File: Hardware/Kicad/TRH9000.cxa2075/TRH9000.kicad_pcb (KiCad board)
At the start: 4 copper layers, 100 x 77.5 mm, 66 parts, among them J1 S-Video, J2 RGB, Q1 BC817, U1 74HC138, U2 74HC32, U3 V9990, U4 KM428C256, U5 KM428C256, U6 CXA2075M, X1 14.31818MHz, Y1 21.47727Mhz

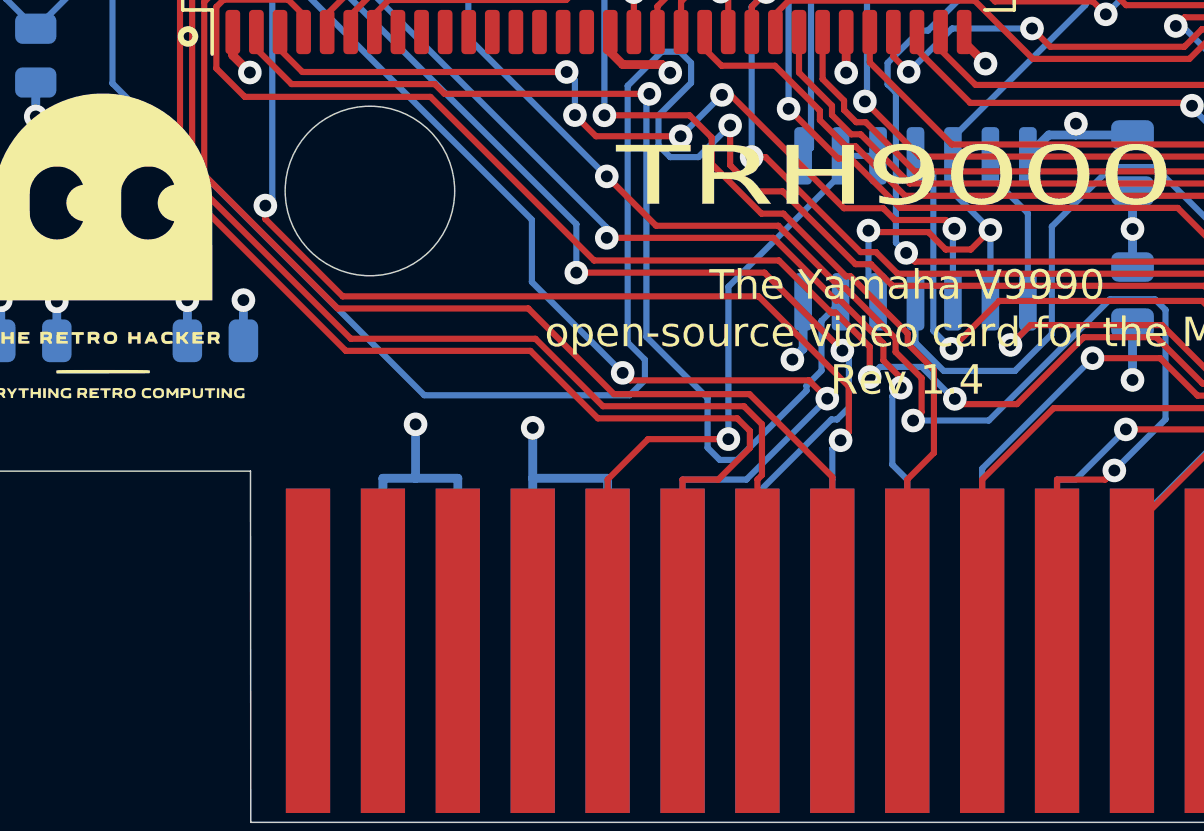
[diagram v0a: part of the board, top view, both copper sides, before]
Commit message: SW1-SW2 jumper. v1.41
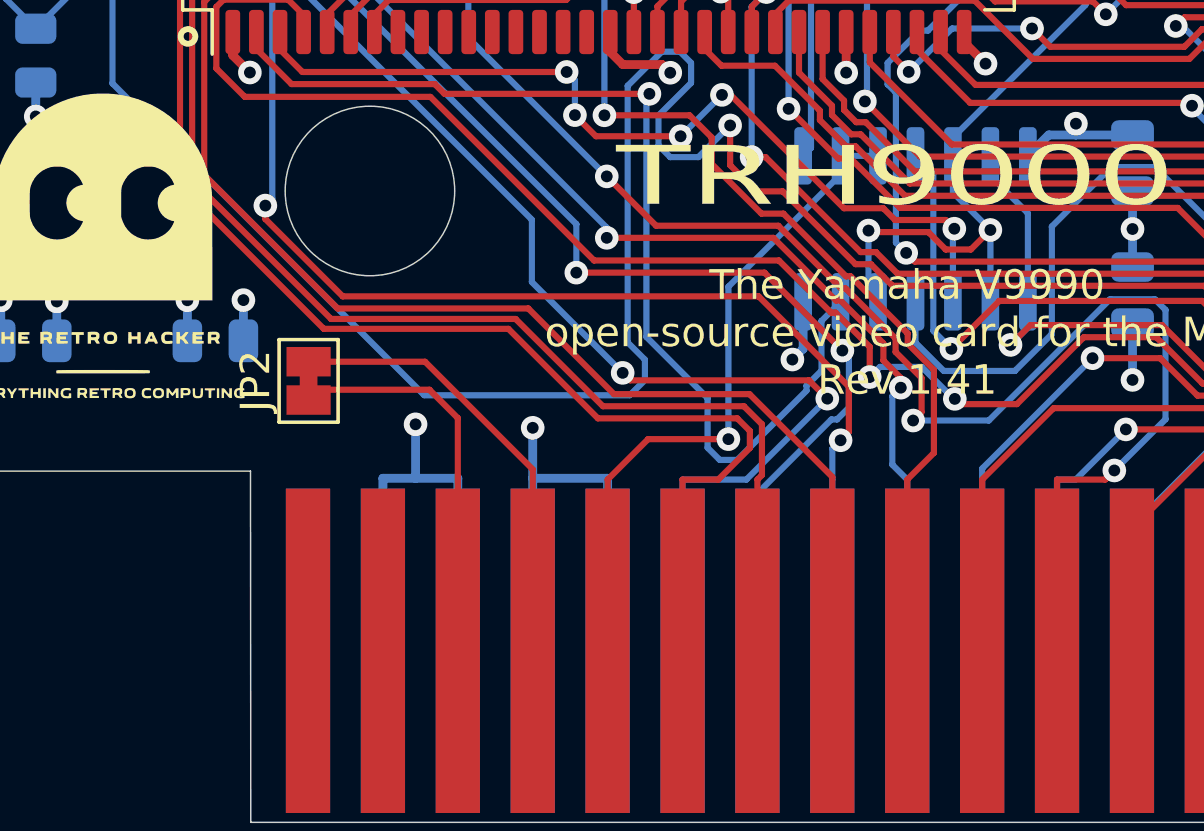
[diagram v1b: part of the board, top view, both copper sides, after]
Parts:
- added JP2: Jumper_2_Bridged, Jumper:SolderJumper-2_P1.3mm_Bridged_Pad1.0x1.5mm, F.Cu at (126.6, 118.5)
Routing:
- net /SW1: track 0.00 -> 15.3 mm
- net /SW2: track 0.00 -> 13.5 mm
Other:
- board text added: "The Yamaha V9990 open-source video card for the MSX Rev 1.41"
- board text removed: "The Yamaha V9990 open-source video card for the MSX Rev 1.4"
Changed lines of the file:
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@@
   (paper "A4")
   (title_block
-    (date "2023-11-05")
-    (rev "1.4")
+    (date "2023-12-31")
+    (rev "1.41")
     (company "The Retro Hacker")
     (comment 2 "Shared under CERN-OHL-S license")
@@
     )
   )
+  (footprint "Jumper:SolderJumper-2_P1.3mm_Bridged_Pad1.0x1.5mm" (layer "F.Cu")
+    (at 126.6 118.5 90)
+    (descr "SMD Solder Jumper, 1x1.5mm Pads, 0.3mm gap, bridged with 1 copper strip")
+    (tags "net tie solder jumper bridged")
+    (property "Sheetfile" "TRH9000.kicad_sch")
+    (property "Sheetname" "")
+    (property "ki_description" "Jumper, 2-pole, closed/bridged")
+    (property "ki_keywords" "Jumper SPST")
+    (attr exclude_from_pos_files)
+    (net_tie_pad_groups "1, 2")
+    (fp_text reference "JP2" (at 0 -1.8 90) (layer "F.SilkS")
+        (effects (font (size 1 1) (thickness 0.15)))
+    )
+    (fp_text value "Jumper_2_Bridged" (at 0 1.9 90) (layer "F.Fab") hide
+        (effects (font (size 1 1) (thickness 0.15)))
+    )
+    (fp_poly
+      (pts
+        (xy -0.25 -0.3)
+        (xy 0.25 -0.3)
+        (xy 0.25 0.3)
+        (xy -0.25 0.3)
+      )
+      (stroke (width 0) (type solid)) (fill solid) (layer "F.Cu"))
+    (fp_line (start -1.4 -1) (end 1.4 -1)
+      (stroke (width 0.12) (type solid)) (layer "F.SilkS"))
+    (fp_line (start -1.4 1) (end -1.4 -1)
+      (stroke (width 0.12) (type solid)) (layer "F.SilkS"))
+    (fp_line (start 1.4 -1) (end 1.4 1)
+      (stroke (width 0.12) (type solid)) (layer "F.SilkS"))
+    (fp_line (start 1.4 1) (end -1.4 1)
+      (stroke (width 0.12) (type solid)) (layer "F.SilkS"))
+    (fp_line (start -1.65 -1.25) (end -1.65 1.25)
+      (stroke (width 0.05) (type solid)) (layer "F.CrtYd"))
+    (fp_line (start -1.65 -1.25) (end 1.65 -1.25)
+      (stroke (width 0.05) (type solid)) (layer "F.CrtYd"))
+    (fp_line (start 1.65 1.25) (end -1.65 1.25)
+      (stroke (width 0.05) (type solid)) (layer "F.CrtYd"))
+    (fp_line (start 1.65 1.25) (end 1.65 -1.25)
+      (stroke (width 0.05) (type solid)) (layer "F.CrtYd"))
+    (pad "1" smd rect (at -0.65 0 90) (size 1 1.5) (layers "F.Cu" "F.Mask")
+      (net 27 "/SW2") (pinfunction "A") (pintype "passive"))
+    (pad "2" smd rect (at 0.65 0 90) (size 1 1.5) (layers "F.Cu" "F.Mask")
+      (net 28 "/SW1") (pinfunction "B") (pintype "passive"))
+  )
   (footprint "Capacitor_SMD:C_0805_2012Metric" (layer "F.Cu")
     (at 195.54 86.21 -90)
@@
     (effects (font (size 1 1) (thickness 0.15)))
   )
-  (gr_text "The Yamaha V9990 \nopen-source video card for the MSX\nRev 1.4" (at 146.9 116.86) (layer "F.SilkS")
+  (gr_text "The Yamaha V9990 \nopen-source video card for the MSX\nRev 1.41" (at 146.9 116.86) (layer "F.SilkS")
     (effects (font (size 1 1) (thickness 0.15)))
   )
@@
   (segment (start 139.28 127.653) (end 139.28 121.8477) (width 0.21) (layer "B.Cu") (net 26))
   (segment (start 120.2258 99.2641) (end 120.4017 99.2641) (width 0.21) (layer "B.Cu") (net 26))
-  (segment (start 134.1222 117.4818) (end 136.4104 119.77) (width 0.21) (layer "F.Cu") (net 29))
-  (segment (start 139.28 127.653) (end 139.28 121.8477) (width 0.21) (layer "F.Cu") (net 29))
-  (segment (start 122.2406 105.3092) (end 122.2406 111.859) (width 0.21) (layer "F.Cu") (net 29))
-  (segment (start 122.2013 98.62) (end 122.6506 99.0693) (width 0.21) (layer "F.Cu") (net 29))
-  (segment (start 136.4104 119.77) (end 141.1359 119.77) (width 0.21) (layer "F.Cu") (net 29))
+  (segment (start 130.7 118.8) (end 131.66 119.76) (width 0.21) (layer "F.Cu") (net 27))
+  (segment (start 126.6 119.15) (end 126.95 118.8) (width 0.21) (layer "F.Cu") (net 27))
+  (segment (start 126.95 118.8) (end 130.7 118.8) (width 0.21) (layer "F.Cu") (net 27))
+  (segment (start 131.66 119.76) (end 131.66 127.653) (width 0.21) (layer "F.Cu") (net 27))
+  (segment (start 130.55 117.85) (end 134.2 121.5) (width 0.21) (layer "F.Cu") (net 28))
+  (segment (start 134.2 121.5) (end 134.2 127.653) (width 0.21) (layer "F.Cu") (net 28))
+  (segment (start 126.6 117.85) (end 130.55 117.85) (width 0.21) (layer "F.Cu") (net 28))
+  (segment (start 139.28 121.8477) (end 139.28 127.653) (width 0.21) (layer "F.Cu") (net 29))
+  (segment (start 140.4917 121.8477) (end 139.28 121.8477) (width 0.21) (layer "F.Cu") (net 29))
+  (segment (start 121.58 98.62) (end 122.2013 98.62) (width 0.21) (layer "F.Cu") (net 29))
   (segment (start 122.6506 104.8992) (end 122.2406 105.3092) (width 0.21) (layer "F.Cu") (net 29))
+  (segment (start 136.4104 119.77) (end 141.1359 119.77) (width 0.21) (layer "F.Cu") (net 29))
+  (segment (start 122.2406 111.859) (end 127.1166 116.735) (width 0.21) (layer "F.Cu") (net 29))
   (segment (start 141.5636 120.1977) (end 141.5636 120.7758) (width 0.21) (layer "F.Cu") (net 29))
-  (segment (start 121.58 98.62) (end 122.2013 98.62) (width 0.21) (layer "F.Cu") (net 29))
-  (segment (start 122.2406 111.859) (end 127.8634 117.4818) (width 0.21) (layer "F.Cu") (net 29))
-  (segment (start 140.4917 121.8477) (end 139.28 121.8477) (width 0.21) (layer "F.Cu") (net 29))
-  (segment (start 127.8634 117.4818) (end 134.1222 117.4818) (width 0.21) (layer "F.Cu") (net 29))
+  (segment (start 133.3754 116.735) (end 136.4104 119.77) (width 0.21) (layer "F.Cu") (net 29))
   (segment (start 122.6506 99.0693) (end 122.6506 104.8992) (width 0.21) (layer "F.Cu") (net 29))
-  (segment (start 141.1359 119.77) (end 141.5636 120.1977) (width 0.21) (layer "F.Cu") (net 29))
   (segment (start 141.5636 120.7758) (end 140.4917 121.8477) (width 0.21) (layer "F.Cu") (net 29))
+  (segment (start 122.2406 105.3092) (end 122.2406 111.859) (width 0.21) (layer "F.Cu") (net 29))
+  (segment (start 127.1166 116.735) (end 133.3754 116.735) (width 0.21) (layer "F.Cu") (net 29))
+  (segment (start 122.2013 98.62) (end 122.6506 99.0693) (width 0.21) (layer "F.Cu") (net 29))
+  (segment (start 141.1359 119.77) (end 141.5636 120.1977) (width 0.21) (layer "F.Cu") (net 29))
+  (segment (start 141.3627 119.3597) (end 141.974 119.971) (width 0.21) (layer "F.Cu") (net 30))
+  (segment (start 133.6207 116.4) (end 136.5804 119.3597) (width 0.21) (layer "F.Cu") (net 30))
   (segment (start 121.58 97.02) (end 122.1445 97.02) (width 0.21) (layer "F.Cu") (net 30))
   (segment (start 122.1445 97.02) (end 123.0609 97.9364) (width 0.21) (layer "F.Cu") (net 30))
-  (segment (start 141.974 121.6937) (end 141.82 121.8477) (width 0.21) (layer "F.Cu") (net 30))
-  (segment (start 122.6509 111.689) (end 128.0333 117.0714) (width 0.21) (layer "F.Cu") (net 30))
-  (segment (start 141.3627 119.3597) (end 141.974 119.971) (width 0.21) (layer "F.Cu") (net 30))
-  (segment (start 141.82 127.653) (end 141.82 121.8477) (width 0.21) (layer "F.Cu") (net 30))
+  (segment (start 141.82 121.8477) (end 141.82 127.653) (width 0.21) (layer "F.Cu") (net 30))
+  (segment (start 127.3619 116.4) (end 133.6207 116.4) (width 0.21) (layer "F.Cu") (net 30))
   (segment (start 123.0609 105.0692) (end 122.6509 105.4792) (width 0.21) (layer "F.Cu") (net 30))
-  (segment (start 134.2921 117.0714) (end 136.5804 119.3597) (width 0.21) (layer "F.Cu") (net 30))
-  (segment (start 123.0609 97.9364) (end 123.0609 105.0692) (width 0.21) (layer "F.Cu") (net 30))
+  (segment (start 122.6509 111.689) (end 127.3619 116.4) (width 0.21) (layer "F.Cu") (net 30))
+  (segment (start 136.5804 119.3597) (end 141.3627 119.3597) (width 0.21) (layer "F.Cu") (net 30))
   (segment (start 141.974 119.971) (end 141.974 121.6937) (width 0.21) (layer "F.Cu") (net 30))
   (segment (start 122.6509 105.4792) (end 122.6509 111.689) (width 0.21) (layer "F.Cu") (net 30))
-  (segment (start 136.5804 119.3597) (end 141.3627 119.3597) (width 0.21) (layer "F.Cu") (net 30))
-  (segment (start 128.0333 117.0714) (end 134.2921 117.0714) (width 0.21) (layer "F.Cu") (net 30))
+  (segment (start 123.0609 97.9364) (end 123.0609 105.0692) (width 0.21) (layer "F.Cu") (net 30))
+  (segment (start 141.974 121.6937) (end 141.82 121.8477) (width 0.21) (layer "F.Cu") (net 30))
   (segment (start 123.4715 95.9355) (end 123.4715 105.2389) (width 0.21) (layer "F.Cu") (net 31))
   (segment (start 121.58 94.62) (end 122.156 94.62) (width 0.21) (layer "F.Cu") (net 31))

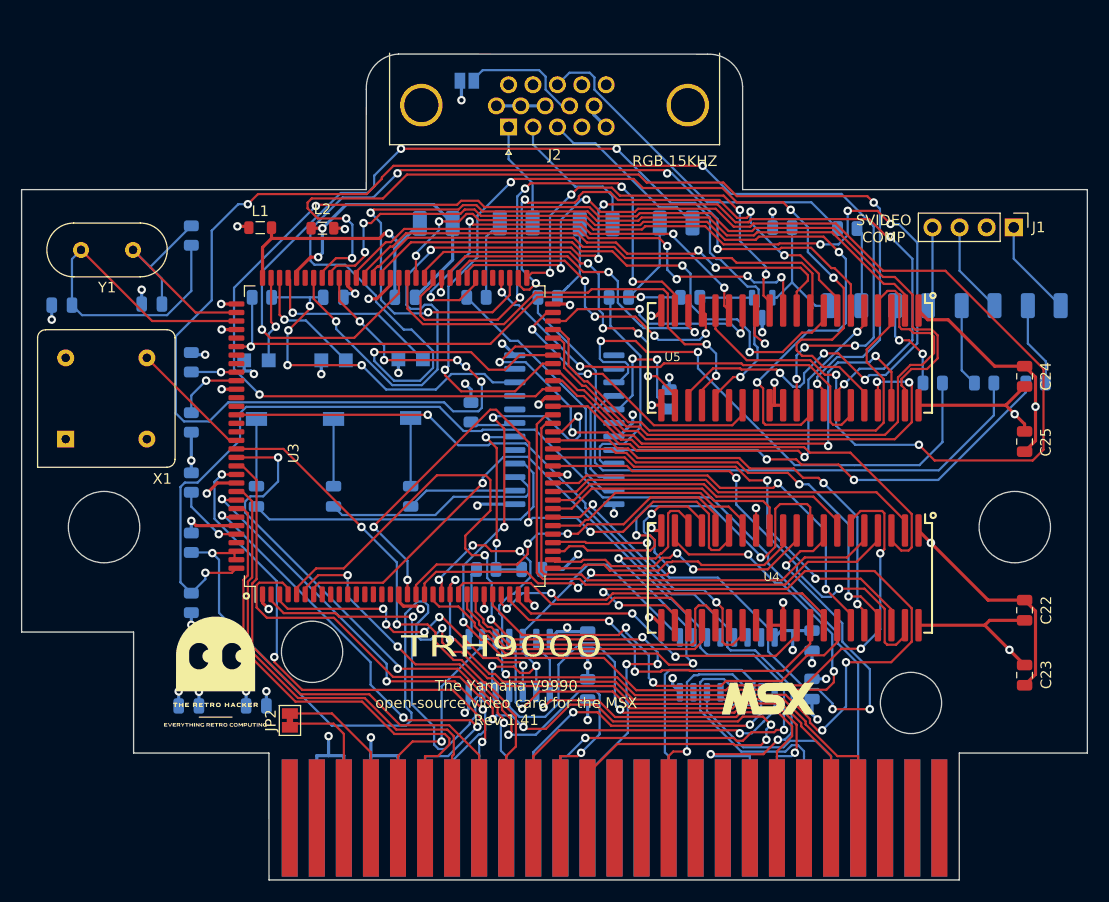
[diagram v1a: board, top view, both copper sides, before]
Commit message: Updates  to have Svideo and Composite exposed via appropriate connectors
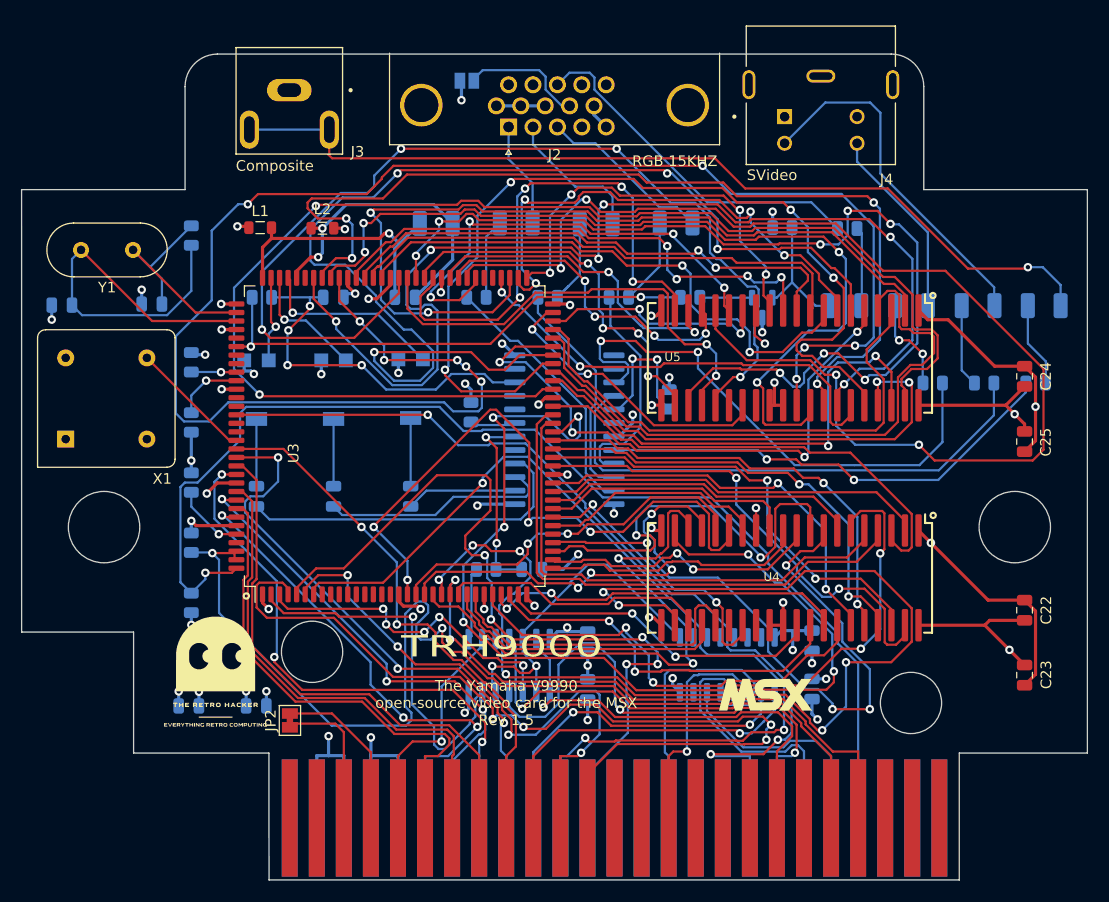
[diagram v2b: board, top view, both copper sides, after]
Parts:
- removed J1: S-Video, Connector_PinHeader_2.54mm:PinHeader_1x04_P2.54mm_Vertical
- removed the REF** at (174.5, 95.6)
- added J3: Composite, Footprints:SWITCHCRAFT_PJRAN1X1U02AUX, F.Cu at (126.5, 59.4)
- added J4: SVideo, Footprints:CUI_MD-40SM, F.Cu at (176.4, 58.0)
- added REF**: OSHW-Logo2_14.6x12mm_SilkScreen, Symbol:OSHW-Logo2_14.6x12mm_SilkScreen, B.Cu at (173.8, 95.0)
- moved MSX1 0.45 mm to (171.2, 116.1)
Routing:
- net /VIDEO/CVOUT: track 9.17 -> 85.7 mm, vias 0 -> 1
- net /VIDEO/YOUT: track 8.70 -> 33.5 mm
- net /VIDEO/COUT: track 7.53 -> 18.0 mm
- net Net-(C9-Pad2): track 8.76 -> 7.45 mm
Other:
- outline, holes or cut-outs redrawn
- board text added: "The Yamaha V9990 open-source video card for the MSX Rev 1.5"
- board text removed: "SVIDEO COMP"
- board text removed: "The Yamaha V9990 open-source video card for the MSX Rev 1.41"

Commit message: Fix on pins 12 and 13 of the VRAM
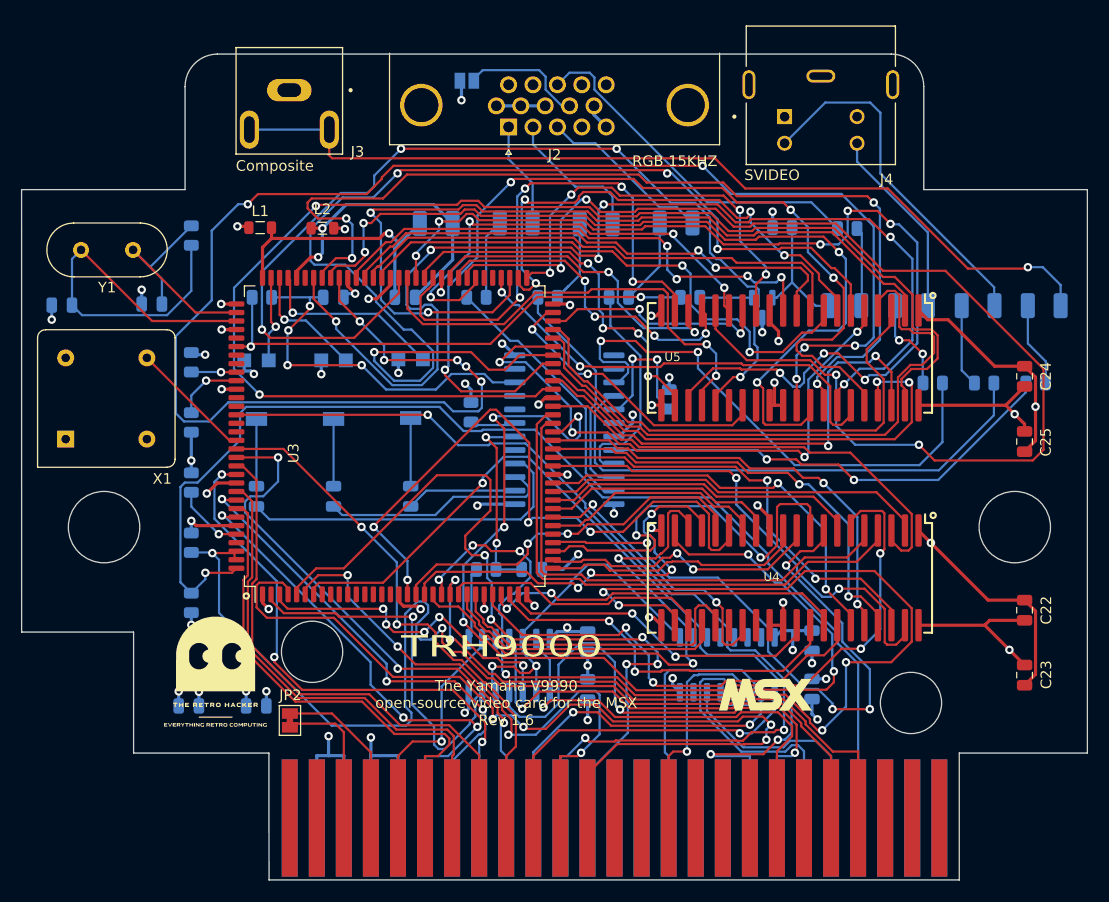
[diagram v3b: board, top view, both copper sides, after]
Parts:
- removed REF**: OSHW-Logo2_14.6x12mm_SilkScreen, Symbol:OSHW-Logo2_14.6x12mm_SilkScreen
- J4: value SVideo -> SVIDEO
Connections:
- U4 pad 12: /VDP/~{V0_WE} -> GND
- U4 pad 13: GND -> /VDP/~{V0_WE}
- U5 pad 12: /VDP/~{V1_WE} -> GND
- U5 pad 13: GND -> /VDP/~{V1_WE}
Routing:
- net /VDP/~{V0_WE}: track 24.0 -> 22.2 mm
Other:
- board text added: "The Yamaha V9990 open-source video card for the MSX Rev 1.6"
- board text removed: "The Yamaha V9990 open-source video card for the MSX Rev 1.5"
